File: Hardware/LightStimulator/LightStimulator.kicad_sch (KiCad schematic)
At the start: 17 parts, among them J1 KK 2 pin, J2 KK 2 pin, J3 KK 4 pin, J4 KK 4 pin, J5 Barrel_Jack, Q1 2N7000, Q2 AOD4184, SW1 SW_SPST, U1 Xiao-ESP32-C3

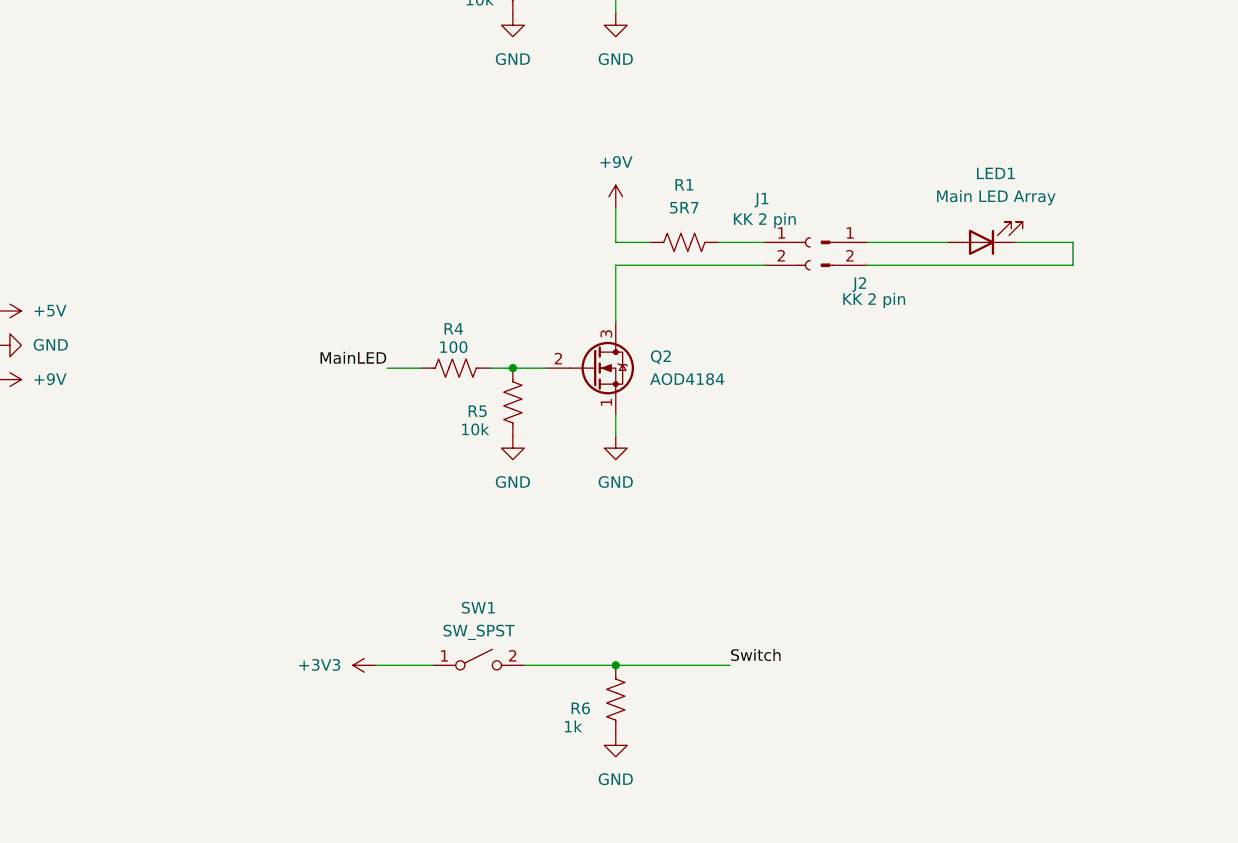
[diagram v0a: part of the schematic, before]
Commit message: Test LED off and corrected schematic.
Removed test LED from code. Corrected the schematic to put a connector in for the switch and hardware the main LED.
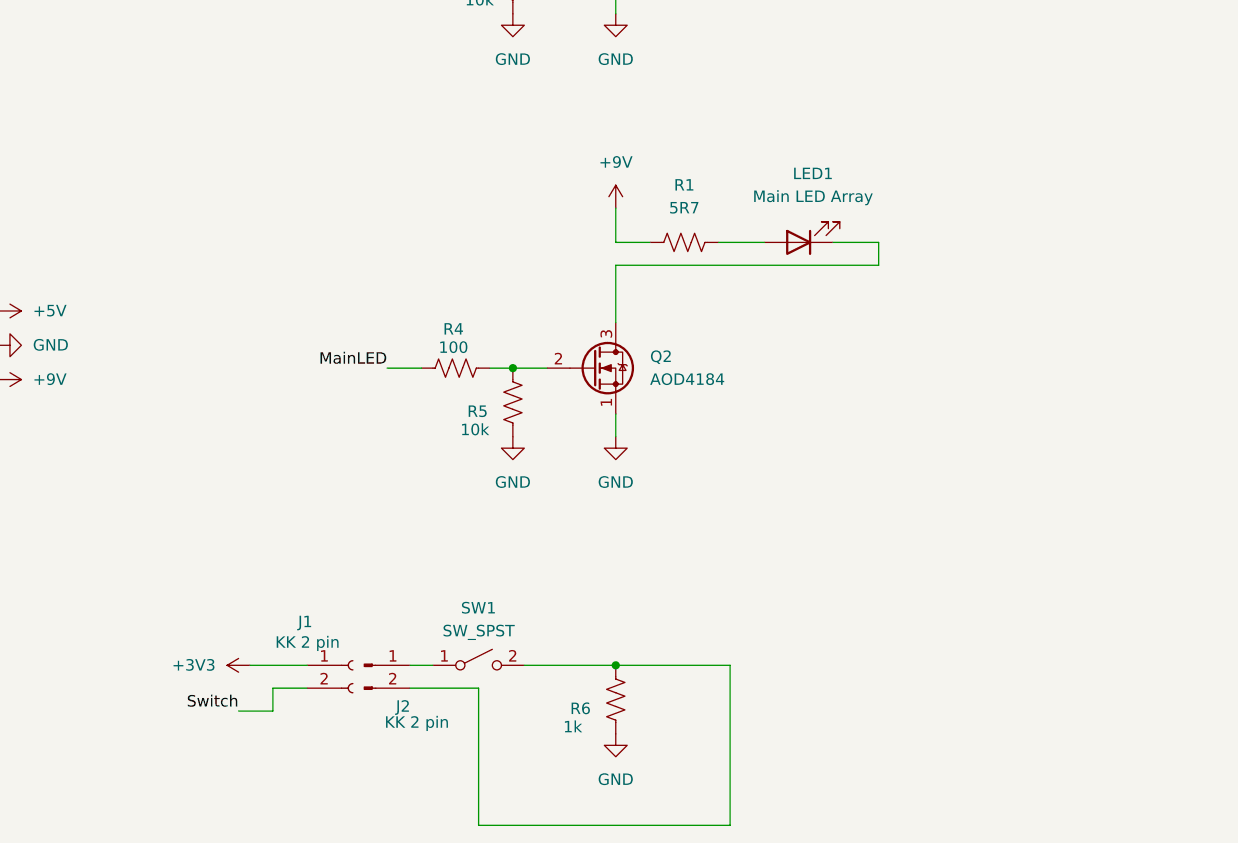
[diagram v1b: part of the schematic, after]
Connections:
- net +3V3: now also J1.1 (Pin_1); no longer SW1.1 (A)
- net Switch: now also J1.2 (Pin_2); no longer R6.1, SW1.2 (B)
- net at LED1.1 (K): now also Q2.3 (D); no longer J2.2 (Pin_2)
- net at LED1.2 (A): now also R1.2; no longer J2.1 (Pin_1)
- new net: J2.1 (Pin_1), SW1.1 (A)
- new net: J2.2 (Pin_2), R6.1, SW1.2 (B)
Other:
- moved on the sheet: J1, J2, LED1
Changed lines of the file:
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@@
 	(wire
 		(pts
-			(xy 203.2 90.17) (xy 212.09 90.17)
+			(xy 49.53 102.87) (xy 49.53 105.41)
 		)
 		(stroke
@@
 	(wire
 		(pts
-			(xy 49.53 102.87) (xy 49.53 105.41)
+			(xy 175.26 92.71) (xy 204.47 92.71)
 		)
 		(stroke
@@
 	(wire
 		(pts
-			(xy 175.26 92.71) (xy 191.77 92.71)
+			(xy 49.53 105.41) (xy 52.07 105.41)
 		)
 		(stroke
@@
 	(wire
 		(pts
-			(xy 49.53 105.41) (xy 52.07 105.41)
+			(xy 204.47 92.71) (xy 204.47 90.17)
+		)
+		(stroke
+			(width 0)
+			(type default)
+		)
+	)
+	(wire
+		(pts
+			(xy 137.16 139.7) (xy 140.97 139.7)
 		)
 		(stroke
@@
 	(wire
 		(pts
+			(xy 133.35 142.24) (xy 137.16 142.24)
+		)
+		(stroke
+			(width 0)
+			(type default)
+		)
+	)
+	(wire
+		(pts
 			(xy 106.68 101.6) (xy 104.14 101.6)
 		)
@@
 	(wire
 		(pts
-			(xy 175.26 43.18) (xy 187.96 43.18)
+			(xy 134.62 137.16) (xy 140.97 137.16)
 		)
 		(stroke
@@
 	(wire
 		(pts
-			(xy 175.26 90.17) (xy 179.07 90.17)
+			(xy 175.26 43.18) (xy 187.96 43.18)
 		)
 		(stroke
@@
 	(wire
 		(pts
-			(xy 104.14 101.6) (xy 104.14 100.33)
+			(xy 175.26 90.17) (xy 179.07 90.17)
 		)
 		(stroke
@@
 	(wire
 		(pts
-			(xy 90.17 102.87) (xy 83.82 102.87)
+			(xy 104.14 101.6) (xy 104.14 100.33)
 		)
 		(stroke
@@
 	(wire
 		(pts
-			(xy 226.06 92.71) (xy 226.06 90.17)
+			(xy 90.17 102.87) (xy 83.82 102.87)
 		)
 		(stroke
@@
 	(wire
 		(pts
-			(xy 85.09 36.83) (xy 95.25 36.83)
+			(xy 160.02 139.7) (xy 152.4 139.7)
 		)
 		(stroke
@@
 	(wire
 		(pts
-			(xy 203.2 92.71) (xy 226.06 92.71)
+			(xy 85.09 36.83) (xy 95.25 36.83)
 		)
 		(stroke
@@
 	(wire
 		(pts
-			(xy 45.72 97.79) (xy 46.99 97.79)
+			(xy 199.39 90.17) (xy 204.47 90.17)
 		)
 		(stroke
@@
 	(wire
 		(pts
-			(xy 226.06 90.17) (xy 219.71 90.17)
+			(xy 45.72 97.79) (xy 46.99 97.79)
 		)
 		(stroke
@@
 	(wire
 		(pts
+			(xy 187.96 154.94) (xy 160.02 154.94)
+		)
+		(stroke
+			(width 0)
+			(type default)
+		)
+	)
+	(wire
+		(pts
 			(xy 87.63 114.3) (xy 87.63 105.41)
 		)
@@
 	(wire
 		(pts
+			(xy 152.4 137.16) (xy 154.94 137.16)
+		)
+		(stroke
+			(width 0)
+			(type default)
+		)
+	)
+	(wire
+		(pts
 			(xy 101.6 105.41) (xy 106.68 105.41)
 		)
@@
 	(wire
 		(pts
+			(xy 137.16 142.24) (xy 137.16 139.7)
+		)
+		(stroke
+			(width 0)
+			(type default)
+		)
+	)
+	(wire
+		(pts
 			(xy 74.93 97.79) (xy 90.17 97.79)
 		)
@@
 	(wire
 		(pts
-			(xy 148.59 137.16) (xy 154.94 137.16)
+			(xy 160.02 154.94) (xy 160.02 139.7)
 		)
 		(stroke
@@
 	(wire
 		(pts
+			(xy 187.96 137.16) (xy 187.96 154.94)
+		)
+		(stroke
+			(width 0)
+			(type default)
+		)
+	)
+	(wire
+		(pts
 			(xy 163.83 104.14) (xy 167.64 104.14)
 		)
@@
 	)
 	(label "Switch"
-		(at 187.96 137.16 0)
+		(at 133.35 142.24 180)
 		(fields_autoplaced yes)
 		(effects
@@
 				(size 1.27 1.27)
 			)
-			(justify left bottom)
+			(justify right bottom)
 		)
 	)
@@
 	(symbol
 		(lib_id "Device:LED")
-		(at 215.9 90.17 180)
+		(at 195.58 90.17 180)
 		(unit 1)
 		(exclude_from_sim no)
@@
 		(fields_autoplaced yes)
 		(property "Reference" "LED1"
-			(at 217.4875 82.55 0)
+			(at 197.1675 82.55 0)
 			(effects
 				(font
@@
 		)
 		(property "Value" "Main LED Array"
-			(at 217.4875 85.09 0)
+			(at 197.1675 85.09 0)
 			(effects
 				(font
@@
 		)
 		(property "Footprint" ""
-			(at 215.9 90.17 0)
+			(at 195.58 90.17 0)
 			(effects
 				(font
@@
 		)
 		(property "Datasheet" "~"
-			(at 215.9 90.17 0)
+			(at 195.58 90.17 0)
 			(effects
 				(font
@@
 		)
 		(property "Description" "Light emitting diode"
-			(at 215.9 90.17 0)
+			(at 195.58 90.17 0)
 			(effects
 				(font
@@
 	(symbol
 		(lib_id "Connector:Conn_01x02_Socket")
-		(at 196.85 90.17 0)
+		(at 146.05 137.16 0)
 		(unit 1)
 		(exclude_from_sim no)
@@
 		(dnp no)
 		(property "Reference" "J1"
-			(at 190.754 85.344 0)
+			(at 139.954 132.334 0)
 			(effects
 				(font
@@
 		)
 		(property "Value" "KK 2 pin"
-			(at 188.214 87.63 0)
+			(at 137.414 134.62 0)
 			(effects
 				(font
@@
 		)
 		(property "Footprint" ""
-			(at 196.85 90.17 0)
+			(at 146.05 137.16 0)
 			(effects
 				(font
@@
 		)
 		(property "Datasheet" "~"
-			(at 196.85 90.17 0)
+			(at 146.05 137.16 0)
 			(effects
 				(font
@@
 		)
 		(property "Description" "Generic connector, single row, 01x02, script generated"
-			(at 196.85 90.17 0)
+			(at 146.05 137.16 0)
 			(effects
 				(font
@@
 	(symbol
 		(lib_id "power:+3V3")
-		(at 148.59 137.16 90)
+		(at 134.62 137.16 90)
 		(unit 1)
 		(exclude_from_sim no)
@@
 		(fields_autoplaced yes)
 		(property "Reference" "#PWR011"
-			(at 152.4 137.16 0)
+			(at 138.43 137.16 0)
 			(effects
 				(font
@@
 		)
 		(property "Value" "+3V3"
-			(at 144.78 137.1599 90)
+			(at 130.81 137.1599 90)
 			(effects
 				(font
@@
 		)
 		(property "Footprint" ""
-			(at 148.59 137.16 0)
+			(at 134.62 137.16 0)
 			(effects
 				(font
@@
 		)
 		(property "Datasheet" ""
-			(at 148.59 137.16 0)
+			(at 134.62 137.16 0)
 			(effects
 				(font
@@
 		)
 		(property "Description" "Power symbol creates a global label with name \"+3V3\""
-			(at 148.59 137.16 0)
+			(at 134.62 137.16 0)
 			(effects
 				(font
@@
 	(symbol
 		(lib_id "Connector:Conn_01x02_Pin")
-		(at 198.12 90.17 0)
+		(at 147.32 137.16 0)
 		(unit 1)
 		(exclude_from_sim no)
@@
 		(dnp no)
 		(property "Reference" "J2"
-			(at 202.438 94.742 0)
+			(at 151.638 141.732 0)
 			(effects
 				(font
@@
 		)
 		(property "Value" "KK 2 pin"
-			(at 203.962 96.52 0)
+			(at 153.162 143.51 0)
 			(effects
 				(font
@@
 		)
 		(property "Footprint" ""
-			(at 198.12 90.17 0)
+			(at 147.32 137.16 0)
 			(effects
 				(font
@@
 		)
 		(property "Datasheet" "~"
-			(at 198.12 90.17 0)
+			(at 147.32 137.16 0)
 			(effects
 				(font
@@
 		)
 		(property "Description" "Generic connector, single row, 01x02, script generated"
-			(at 198.12 90.17 0)
+			(at 147.32 137.16 0)
 			(effects
 				(font
